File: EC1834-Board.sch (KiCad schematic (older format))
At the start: 0 parts

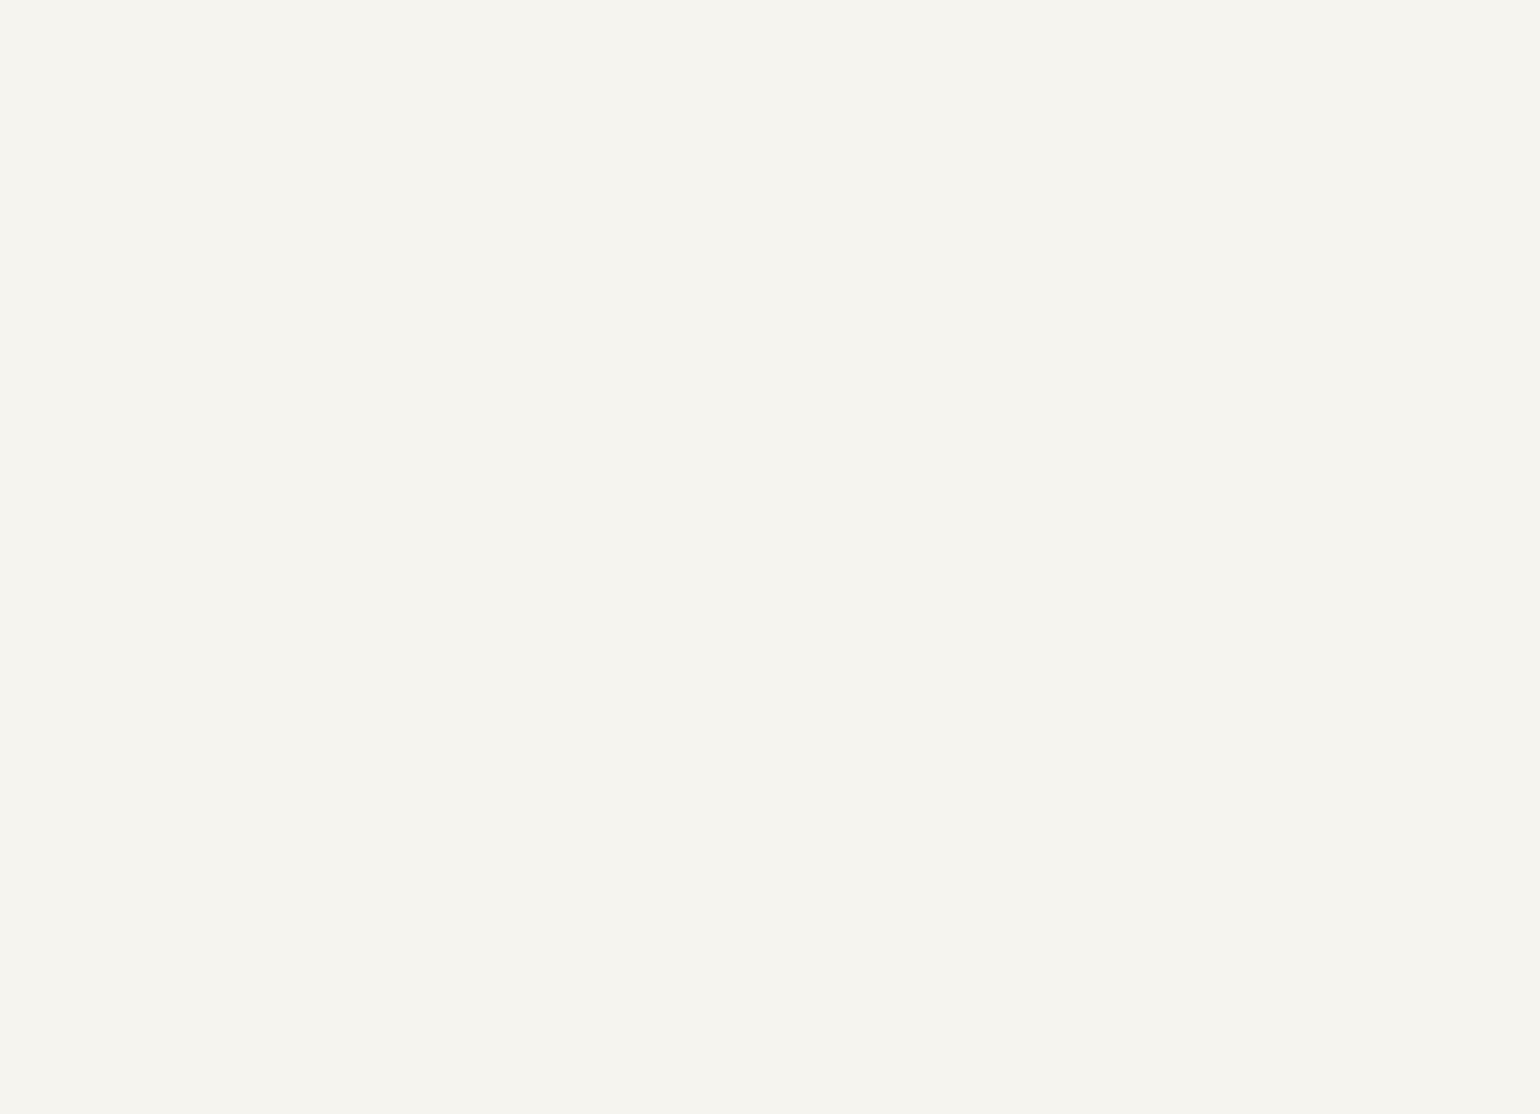
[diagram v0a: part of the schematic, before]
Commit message: Added more ICs Added README
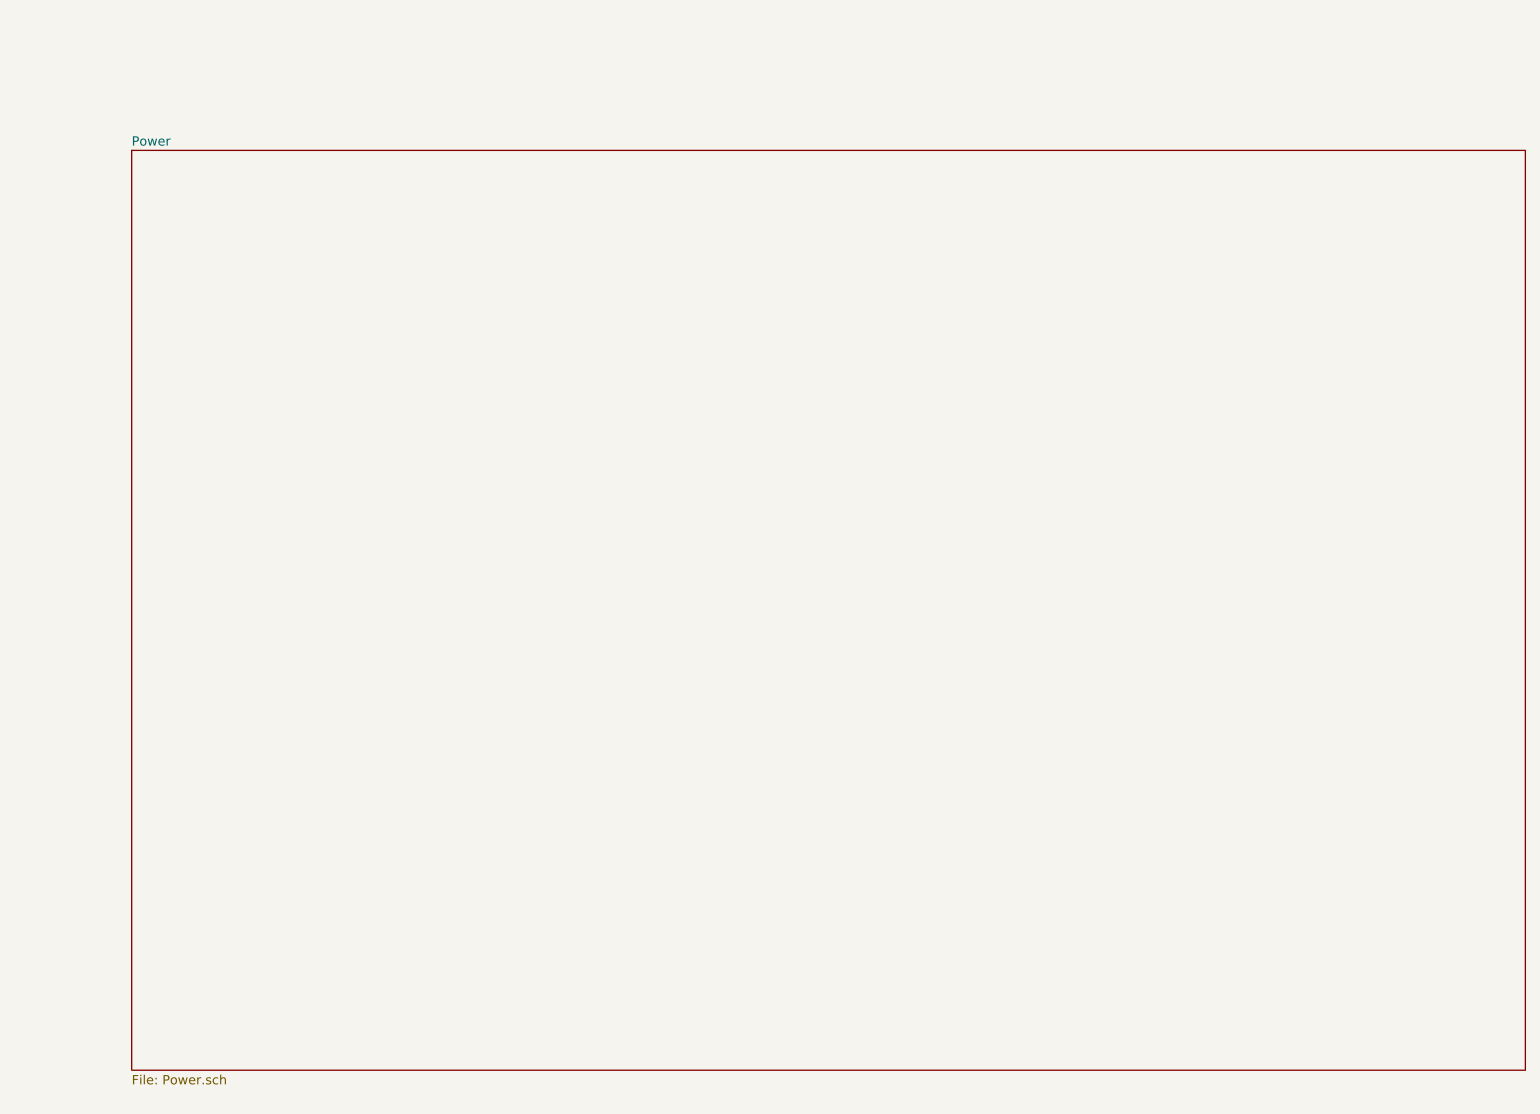
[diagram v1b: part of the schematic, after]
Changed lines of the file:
@@
 $Descr A0 46811 33110
 encoding utf-8
-Sheet 1 4
+Sheet 1 5
 Title ""
 Date ""
@@
 Text Notes 10700 5250 0    404  ~ 0
 Seite 3 - RAM
+$Sheet
+S 10500 12250 7500 4950
+U 63239FAE
+F0 "Power" 50
+F1 "Power.sch" 50
+$EndSheet
 $EndSCHEMATC

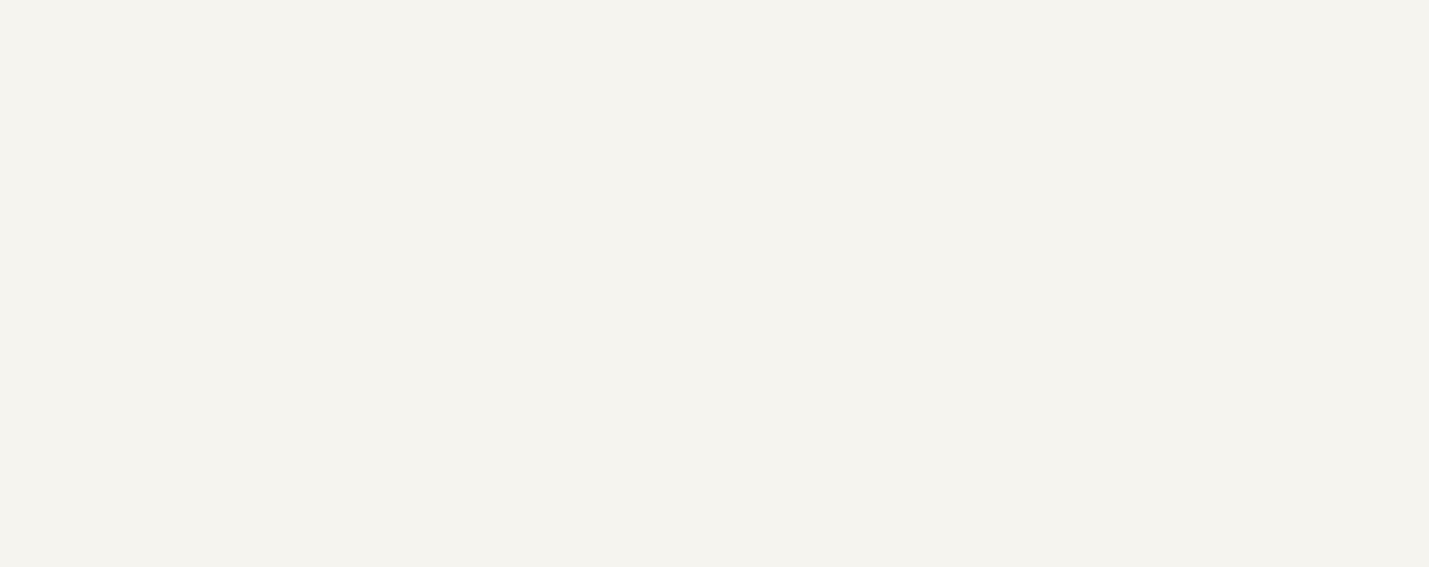
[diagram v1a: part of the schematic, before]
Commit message: Switch to Kicad 6
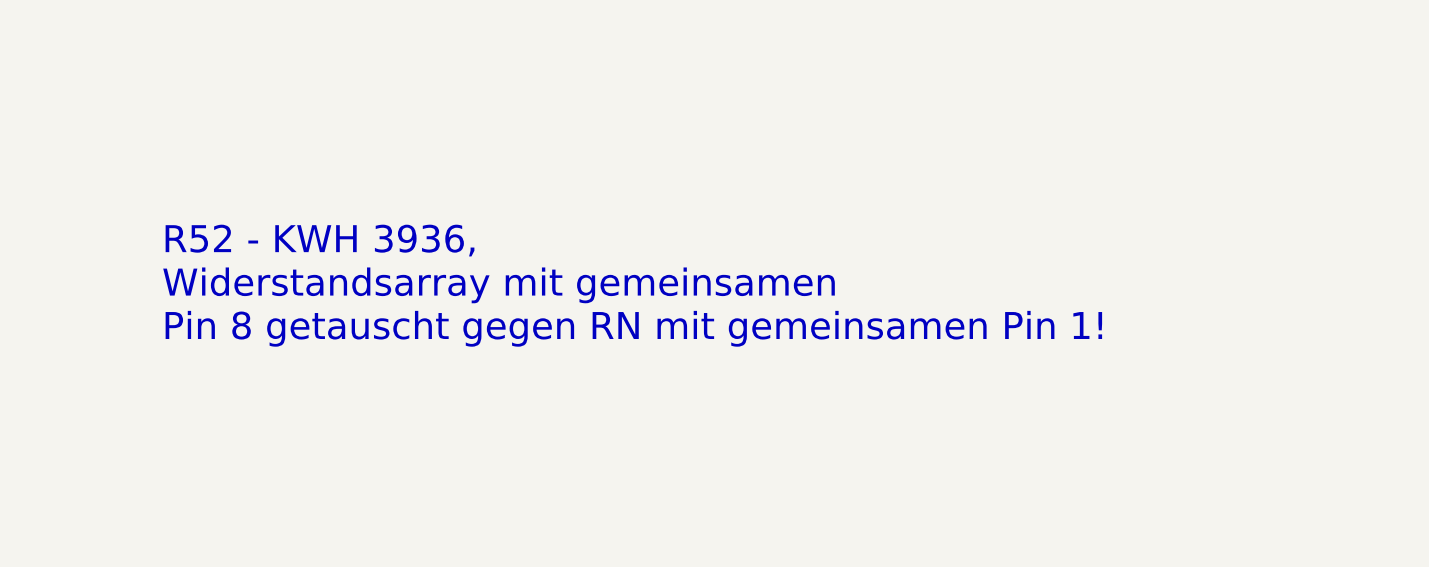
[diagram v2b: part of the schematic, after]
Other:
- note added: "R52 - KWH 3936, \nWiderstandsarray mit gemeinsamen \nPin 8 getauscht gegen RN mit gemeinsamen Pin 1!\n"
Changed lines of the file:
@@
 F1 "Power.sch" 50
 $EndSheet
+Text Notes 19200 6150 0    118  ~ 0
+R52 - KWH 3936, \nWiderstandsarray mit gemeinsamen \nPin 8 getauscht gegen RN mit gemeinsamen Pin 1!\n
 $EndSCHEMATC
